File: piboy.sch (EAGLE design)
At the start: 71 parts, among them CN4 MicroUSB, T1 MMUN2133LT1G, U1 TPS61090RSAR, U2 MCP73871

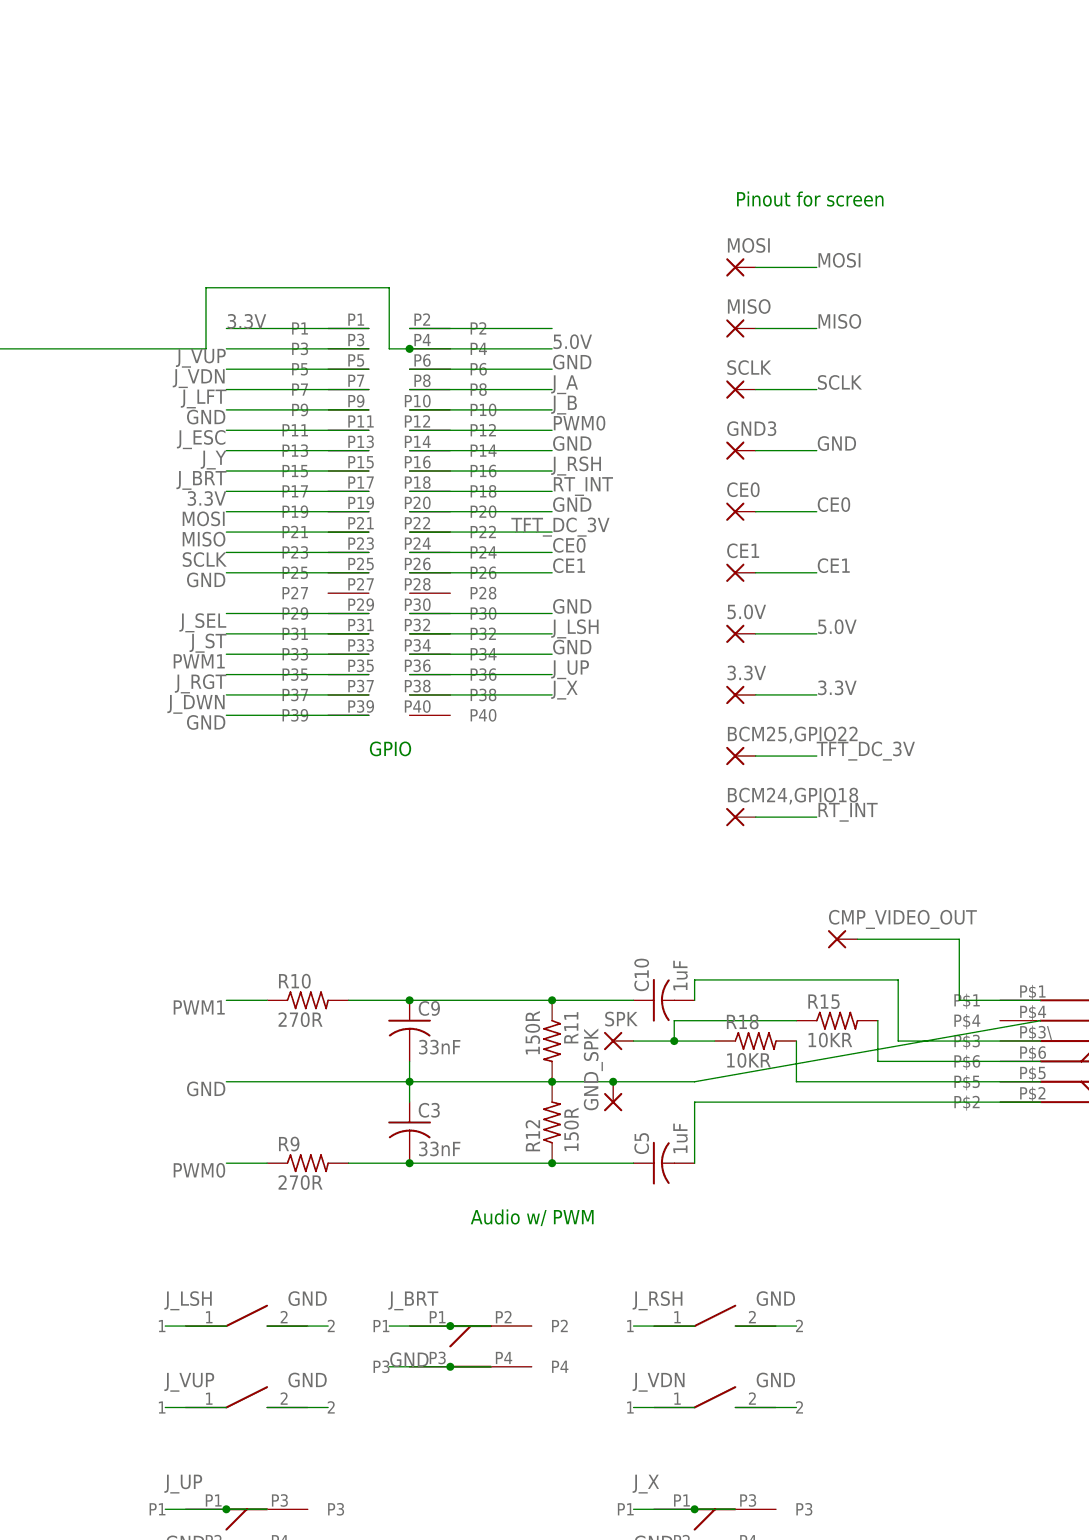
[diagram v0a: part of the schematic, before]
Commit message: TODO: edit device packages to remove silkscreen
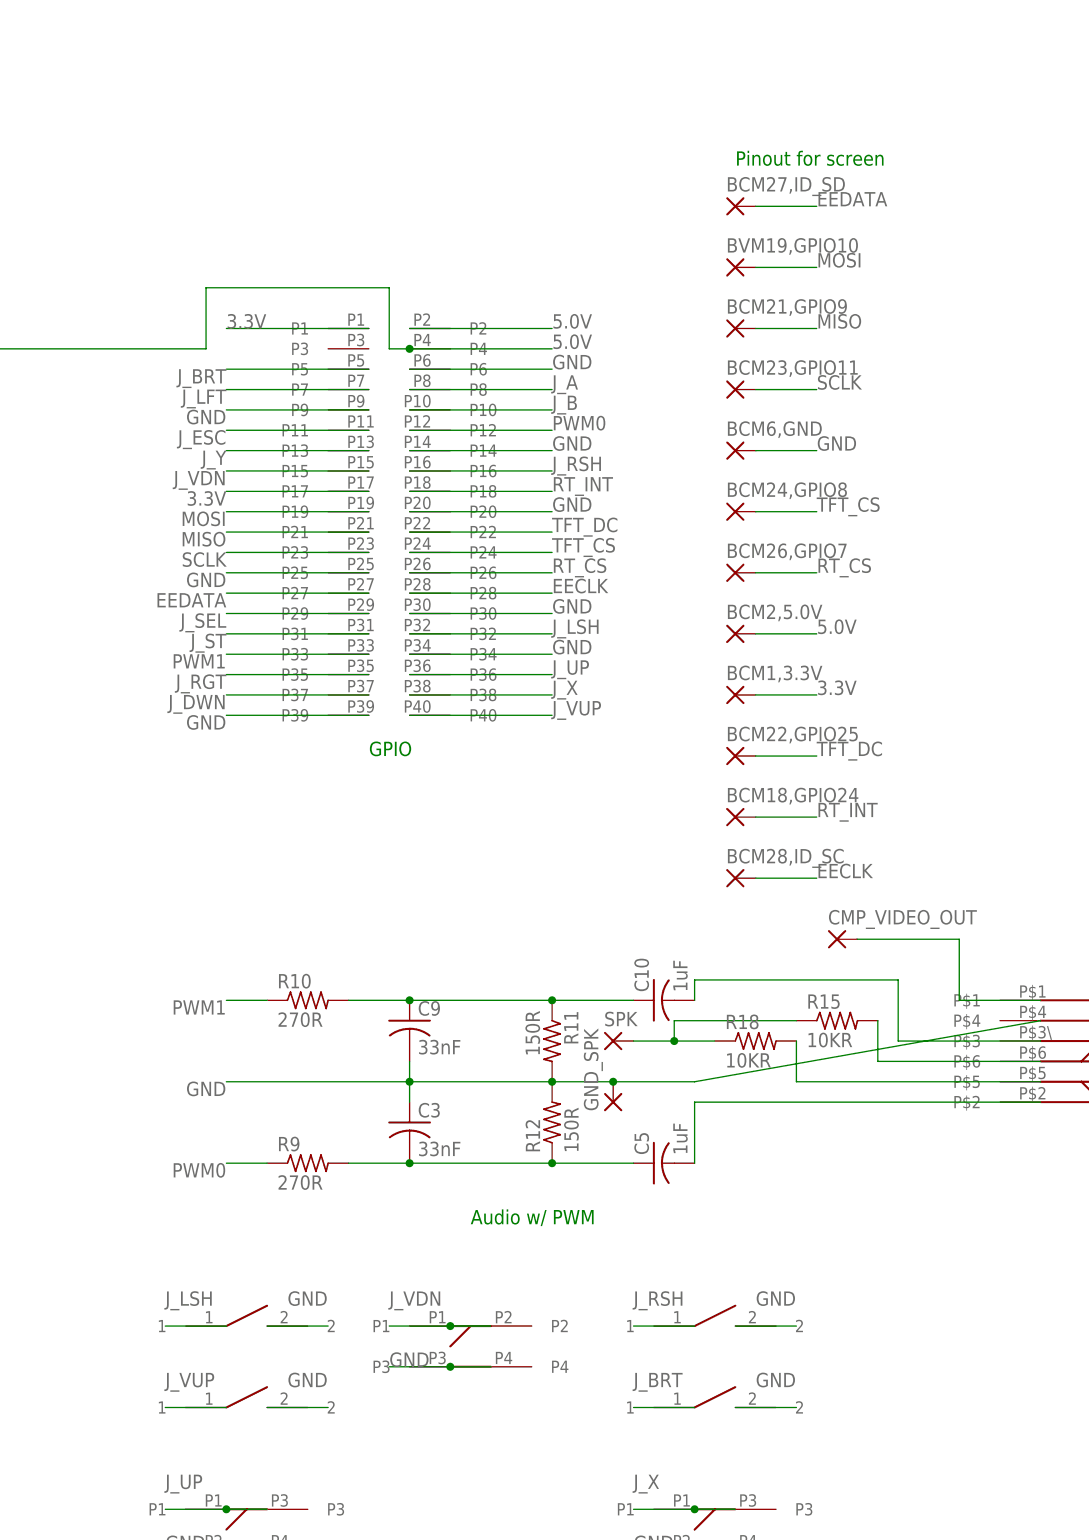
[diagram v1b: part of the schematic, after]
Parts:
- added BCM27,ID_SD, BCM28,ID_SC: (no value), wirepad:1,6/0,9
- renumbered 3.3V to BCM1,3.3V, 5.0V to BCM2,5.0V, BCM24,GPIO18 to BCM18,GPIO24, BCM25,GPIO22 to BCM22,GPIO25, CE0 to BCM24,GPIO8, CE1 to BCM26,GPIO7, GND3 to BCM6,GND, MISO to BCM21,GPIO9, MOSI to BVM19,GPIO10, SCLK to BCM23,GPIO11
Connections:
- net CE0 renamed TFT_CS
- net CE1 renamed RT_CS
- net TFT_DC_3V renamed TFT_DC
- new net EECLK: BCM28,ID_SC.P, U$9.P28
- new net EEDATA: BCM27,ID_SD.P, U$9.P27
- net J_BRT: now also U$30.1, U$9.P5; no longer U$25.P1, U$25.P2, U$9.P15
- net J_VDN: now also U$25.P1, U$25.P2, U$9.P15; no longer U$30.1, U$9.P5
- net J_VUP: now also U$9.P40; no longer U$9.P3

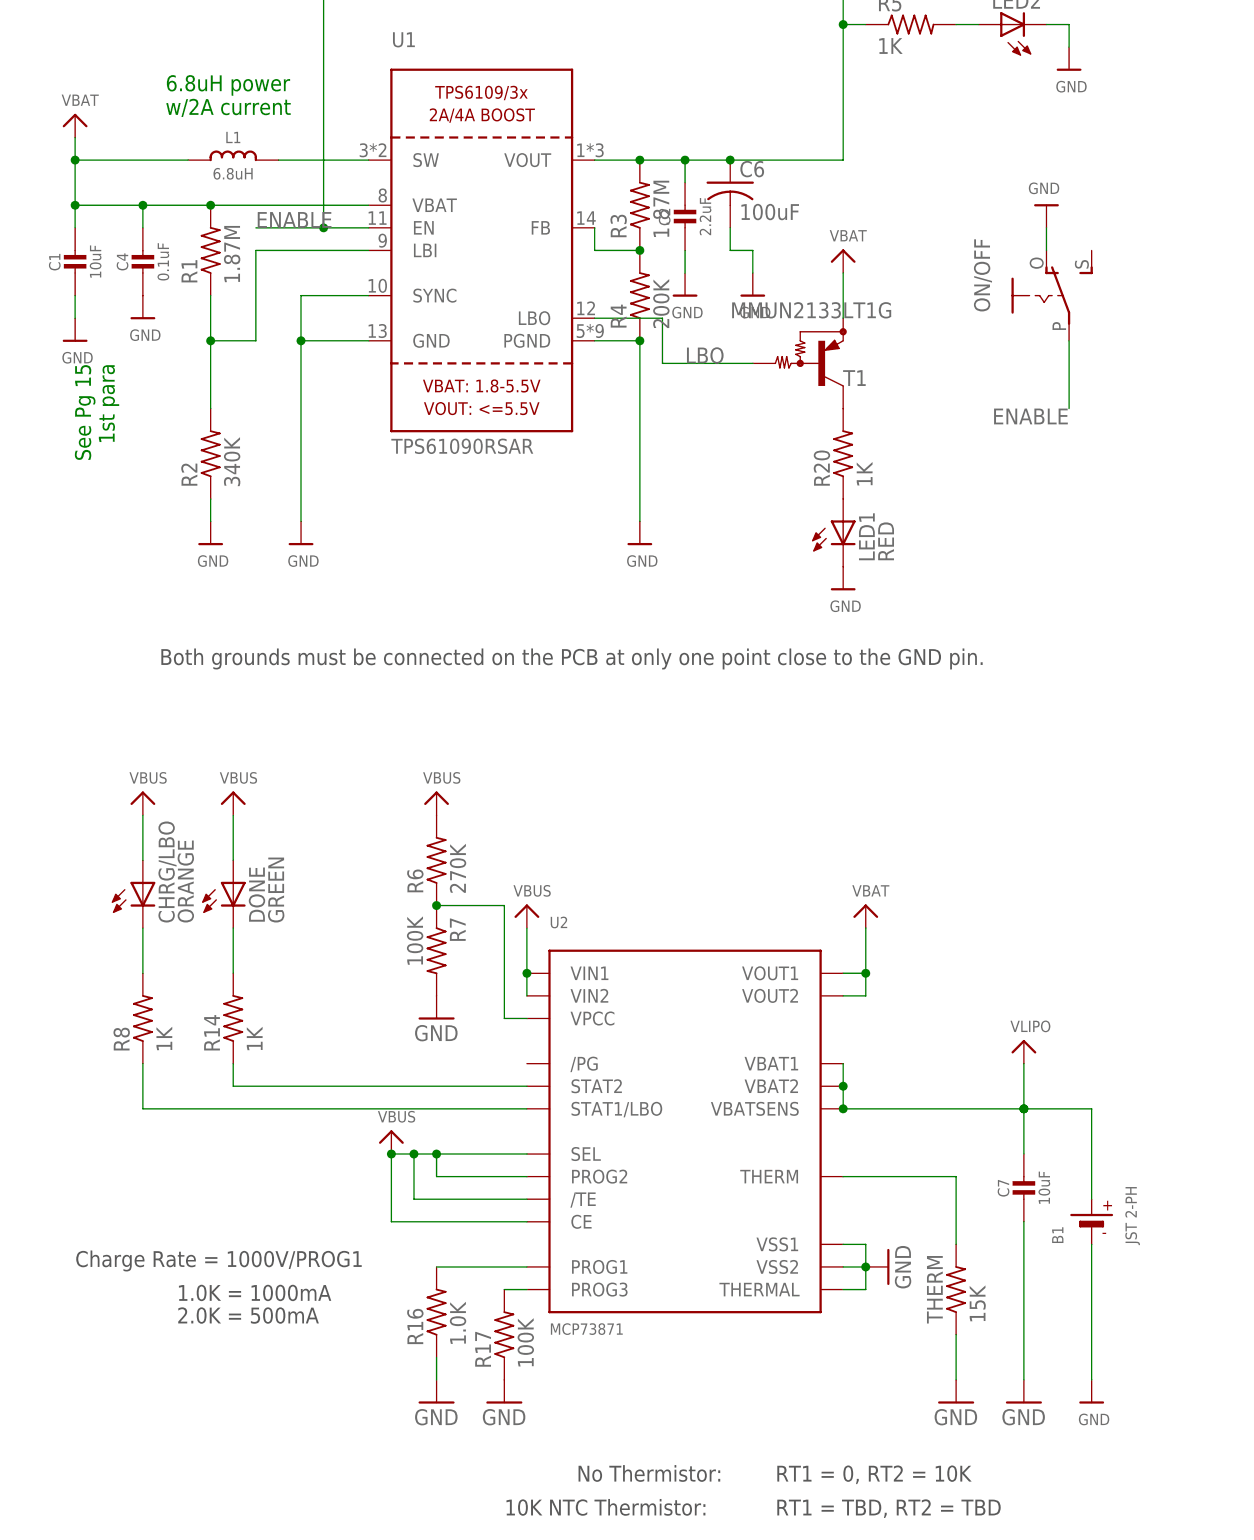
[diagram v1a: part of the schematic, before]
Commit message: -removed all problematic silkscreen -exported all parts into a new library, piboy_new.lbr TODO: Rename piboy_new.lbr
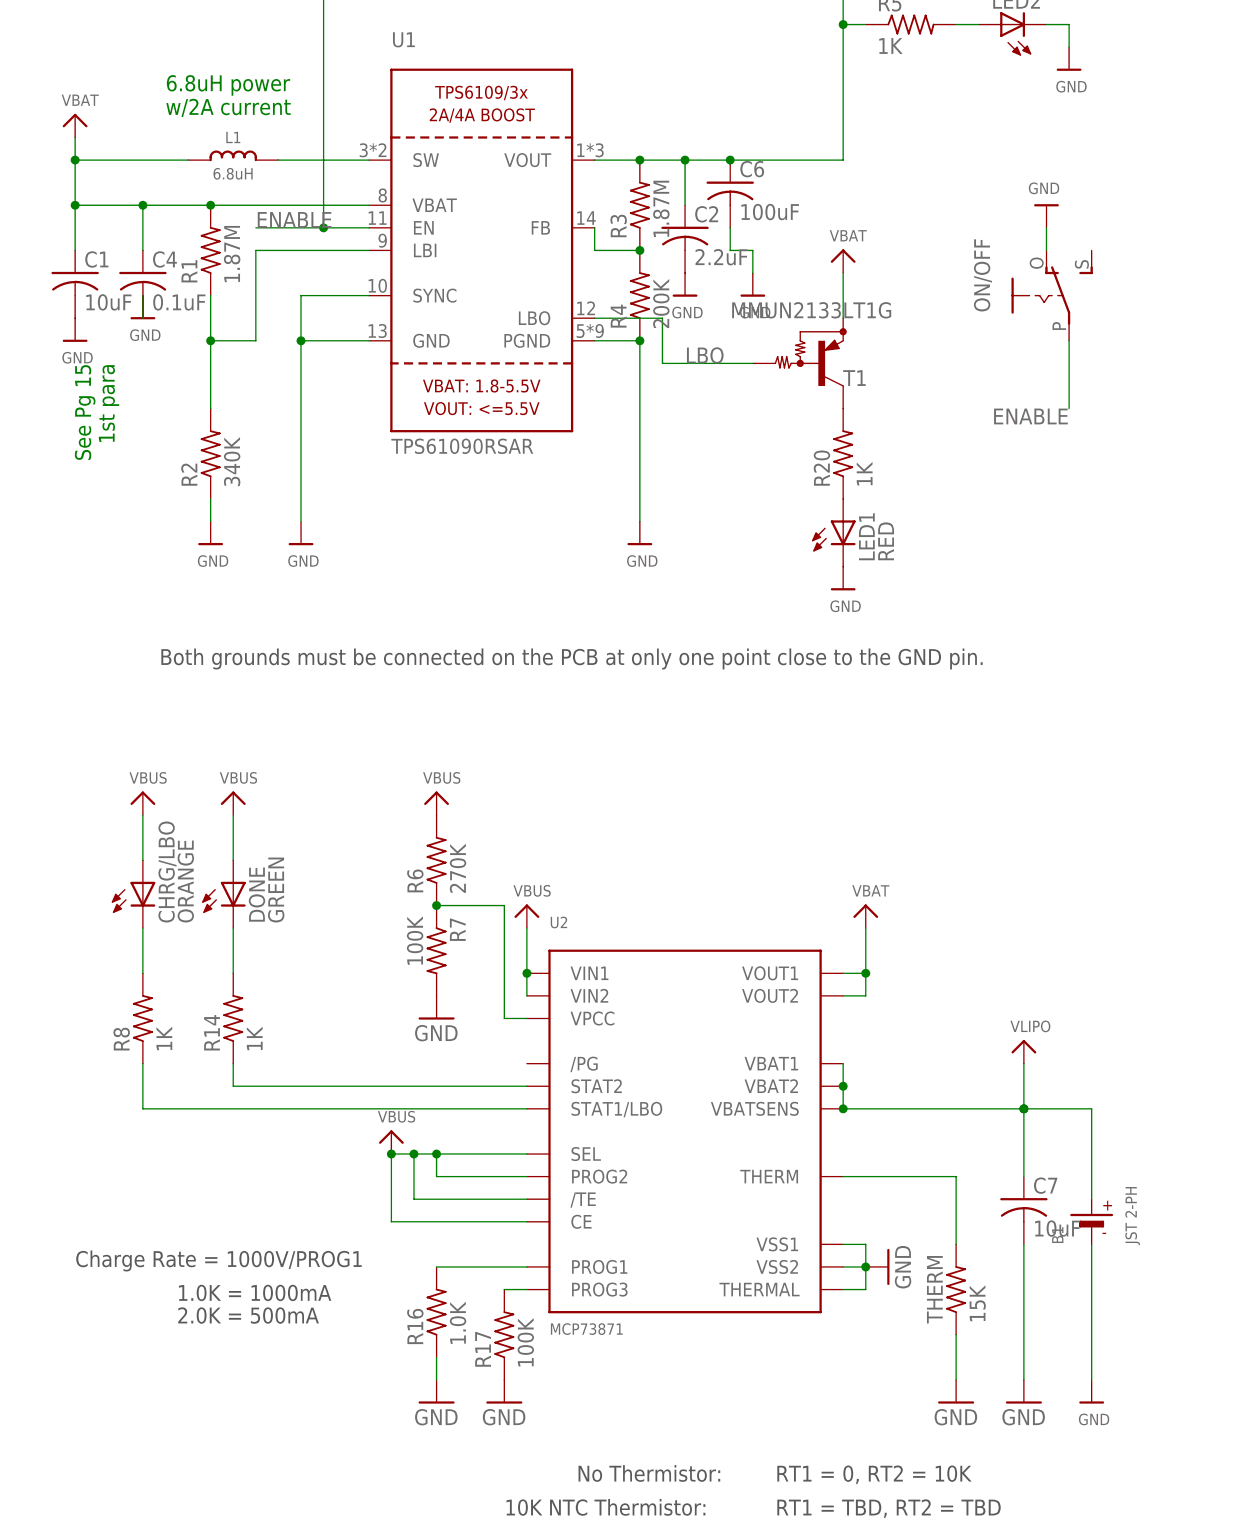
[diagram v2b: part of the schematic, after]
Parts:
- BCM1,3.3V, BCM18,GPIO24, BCM2,5.0V, BCM21,GPIO9, BCM22,GPIO25, BCM23,GPIO11, BCM24,GPIO8, BCM26,GPIO7, BCM27,ID_SD, BCM28,ID_SC, BCM6,GND, BVM19,GPIO10, CMP_VIDEO_OUT, GND_SPK, SPK: device wirepad:1,6/0,9 -> piboy_new:WIREPAD_1,6/0,9
- C1, C2, C7: device microbuilder:CAP_CERAMIC0805-NOOUTLINE -> adafruit:C-USC0805
- C10, C5: device resistor:C-USC0805 -> adafruit:C-USC0805
- C4: device microbuilder:CAP_CERAMIC0805_10MGAP -> adafruit:C-USC0805
- C6: device rcl:C-USC1210 -> adafruit:C-USC1210
- CHRG/LBO, DONE, LED1, LED2: device adafruit:LEDSMT1206 -> piboy_new:ADAFRUIT_LEDCHIPLED_0603
- ON/OFF: device adafruit:EG1218S -> piboy_new:ADAFRUIT_EG1218S
- R1, R10, R11, R12, R13, R14, R15, R16, R17, R18, R2, R20, R3, R4, R5, R6, R7, R8, R9, THERM: device resistor:R-US_R0805 -> adafruit:R-US_R0805
- U$26, U$28, U$29, U$30: value TL1105L-4,3 -> SWITCH_TL1105L-4,3; device switch:TL1105L-4,3 -> piboy_new:SWITCH_TL1105L-4,3
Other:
- moved on the sheet: C1, C2, C4, C7

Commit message: -redid audio circuit -moved around components on the board -began silkscreen -cleared clearance, overlap, airwire DRC -checked component values
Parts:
- removed C10, C5: 1uF, adafruit:C-USC0805
- removed C9: 33nF, adafruit:C-USC0805
- removed GND_SPK, SPK: (no value), piboy_new:WIREPAD_1,6/0,9
- removed R10, R9: 270R, adafruit:R-US_R0805
- removed R11, R12: 150R, adafruit:R-US_R0805
- removed R15, R18: 10KR, adafruit:R-US_R0805
- removed U$29: SWITCH_TL1105L-4,3, piboy_new:SWITCH_TL1105L-4,3
- added C11, C12: 1uf, piboy_new:ADAFRUIT_C-USC0805
- added C13: 10uf, piboy_new:ADAFRUIT_C-USC0805
- added C14, C15: 220pf, piboy_new:ADAFRUIT_C-USC0805
- added FB1, FB2: 100 Ohm @ 100 Mhz, piboy_new:ADAFRUIT_R-US_R0805
- added R19, R21: 100, piboy_new:ADAFRUIT_R-US_R0805
- added R22: 10k, piboy_new:ADAFRUIT_R-US_R0805
- added SPK1, SPK2: (no value), piboy_new:WIREPAD_1,6/0,9
- added U$33: RK10J12R0A0B, piboy_new:RK10J12R0A0B
- added U$40: SJ-43504-SMT-TR, SJ-43504-SMT-TR:SJ-43504-SMT-TR
- C3: value 33nF -> 100nf; device adafruit:C-USC0805 -> piboy_new:ADAFRUIT_C-USC0805
- C8: device microbuilder:CAP_CERAMIC0805-NOOUTLINE -> piboy_new:ADAFRUIT_C-USC0805
- T1: device transistor:MUN2114T1-PNP_DRIVER-SC59-BEC -> piboy_new:TRANSISTOR_MUN2113T1-PNP_DRIVER-SC59-BEC
- U$31: value SJ-43504-SMT-TR -> PAM8302A; device SJ-43504-SMT-TR:SJ-43504-SMT-TR -> piboy_new:PAM8302A
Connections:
- removed net LEFT_HDPHN: C5.2, U$31.P$2
- removed net LEFT_SPEAKER: R18.2, U$31.P$5
- removed net N$14: C10.1, C9.1, R10.2, R11.1
- removed net N$19: C3.2, C5.1, R12.1, R9.2
- removed net N$24: R15.1, R18.1, SPK.P
- removed net RIGHT_HDPHN: C10.2, U$31.P$3
- removed net RIGHT_SPEAKER: R15.2, U$31.P$6
- new net AUD+: SPK2.P, U$40.P$5, U$40.P$6
- new net AUD-: C15.1, FB1.2, SPK1.P, U$40.P$4
- new net N$17: C12.1, R21.1
- new net N$18: R21.2, U$31.IN-\
- new net N$20: C11.1, R19.1
- new net N$21: R19.2, U$31.IN+
- new net N$22: R22.2, U$31.SD\
- new net N$23: FB1.1, U$31.VO-
- new net N$25: C11.2, U$33.P$2
- new net N$26: C12.2, U$33.P$1
- new net N$27: FB2.1, U$31.VO+
- new net N$29: C14.1, C3.1, FB2.2, U$40.P$2, U$40.P$3
- net 5.0V: now also C13.1, R22.1, U$31.VCC
- net CMP_VIDEO_OUT: now also U$40.P$1; no longer U$31.P$1
- net GND: now also C13.2, C14.2, C15.2, C3.2, U$31.GND; no longer C3.1, C9.2, GND_SPK.P, R11.2, R12.2, U$29.2, U$31.P$4
- net J_VUP: no longer U$29.1
- net PWM0: now also U$33.P$3; no longer R9.1
- net PWM1: no longer R10.1
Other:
- moved on the sheet: CMP_VIDEO_OUT

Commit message: -finished silkscreen -done before copper pours
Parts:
- renumbered LED1 to LBO, LED2 to ON
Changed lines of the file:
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@@
 <part name="C2" library="adafruit" deviceset="C-US" device="C0805" value="2.2uF"/>
 <part name="U$19" library="microbuilder" deviceset="VBAT" device=""/>
-<part name="LED1" library="piboy_new" deviceset="ADAFRUIT_LED" device="CHIPLED_0603" value="RED"/>
+<part name="LBO" library="piboy_new" deviceset="ADAFRUIT_LED" device="CHIPLED_0603" value="RED"/>
 <part name="R20" library="adafruit" deviceset="R-US_" device="R0805" value="1K"/>
-<part name="LED2" library="piboy_new" deviceset="ADAFRUIT_LED" device="CHIPLED_0603" value="BLUE"/>
+<part name="ON" library="piboy_new" deviceset="ADAFRUIT_LED" device="CHIPLED_0603" value="BLUE"/>
 <part name="R5" library="adafruit" deviceset="R-US_" device="R0805" value="1K"/>
 <part name="R13" library="adafruit" deviceset="R-US_" device="R0805" value="200K"/>
@@
 <instance part="C2" gate="G$1" x="-86.36" y="-15.24"/>
 <instance part="U$19" gate="G$1" x="-154.94" y="-2.54"/>
-<instance part="LED1" gate="G$1" x="-68.58" y="-48.26"/>
+<instance part="LBO" gate="G$1" x="-68.58" y="-48.26"/>
 <instance part="R20" gate="G$1" x="-68.58" y="-40.64" rot="R90"/>
-<instance part="LED2" gate="G$1" x="-50.8" y="7.62" rot="R90"/>
+<instance part="ON" gate="G$1" x="-50.8" y="7.62" rot="R90"/>
 <instance part="R5" gate="G$1" x="-60.96" y="7.62"/>
 <instance part="R13" gate="G$1" x="-127" y="25.4" rot="R270"/>
@@
 <wire x1="-43.18" y1="7.62" x2="-43.18" y2="5.08" width="0.1524" layer="91"/>
 <pinref part="U$14" gate="G$1" pin="GND"/>
-<pinref part="LED2" gate="G$1" pin="C"/>
+<pinref part="ON" gate="G$1" pin="C"/>
 <wire x1="-45.72" y1="7.62" x2="-43.18" y2="7.62" width="0.1524" layer="91"/>
 </segment>
@@
 </segment>
 <segment>
-<pinref part="LED1" gate="G$1" pin="C"/>
+<pinref part="LBO" gate="G$1" pin="C"/>
 <pinref part="U$20" gate="G$1" pin="GND"/>
 </segment>
@@
 <net name="N$2" class="0">
 <segment>
-<pinref part="LED1" gate="G$1" pin="A"/>
+<pinref part="LBO" gate="G$1" pin="A"/>
 <pinref part="R20" gate="G$1" pin="1"/>
 </segment>
@@
 <segment>
 <pinref part="R5" gate="G$1" pin="2"/>
-<pinref part="LED2" gate="G$1" pin="A"/>
+<pinref part="ON" gate="G$1" pin="A"/>
 <wire x1="-55.88" y1="7.62" x2="-53.34" y2="7.62" width="0.1524" layer="91"/>
 </segment>
